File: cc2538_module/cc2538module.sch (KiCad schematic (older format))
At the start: 49 parts, among them CON1 USB-MICRO-B, J2 XBEE, P1 CONN_2, SW1 JS102011SCQN, U1 TPS769XX, U2 TPS6217X, U3 CC2538, X1 32MHZ, X2 32.768KHz, j9 JTAG

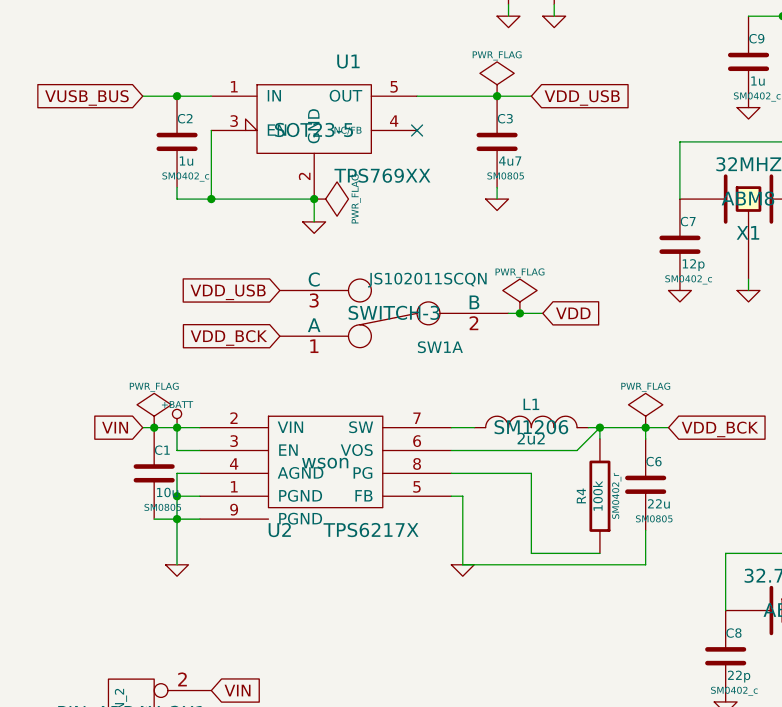
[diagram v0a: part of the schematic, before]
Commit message: Update component tolerances
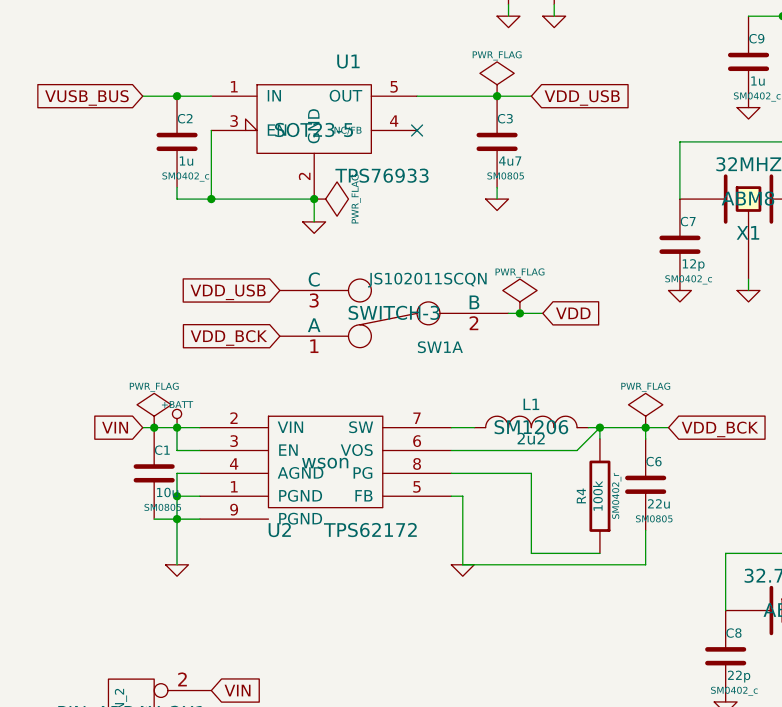
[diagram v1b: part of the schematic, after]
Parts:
- C10, C11, C12, C13, C14, C15, C16, C17, C18, C19, C20, C21, C22, C7, C8, C9: Voltage (none) -> 3.3
- C4, C5: Voltage (none) -> 5
- D1: Color (none) -> red; Voltage (none) -> ~1.6
- D2, D3: Color (none) -> green; Voltage (none) -> 2
- D4: Color (none) -> Green; Voltage (none) -> 2
- U1: value TPS769XX -> TPS76933; Voltage (none) -> 3.3
- U2: value TPS6217X -> TPS62172; Voltage (none) -> 3.3
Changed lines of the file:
@@
 LIBS:contrib
 LIBS:valves
+LIBS:cc2538
+LIBS:cc2538module-cache
+LIBS:jtagx7
+LIBS:tps6217x
 LIBS:w_connectors
-LIBS:cc2538
-LIBS:tps6217x
 LIBS:xbee
-LIBS:jtagx7
-LIBS:cc2538module-cache
 EELAYER 27 0
 EELAYER END
@@
 Sheet 1 1
 Title ""
-Date "30 jul 2014"
+Date "1 aug 2014"
 Rev ""
 Comp ""
@@
 F 2 "SM0402_c" H 2838 1600 30  0000 C CNN
 F 3 "~" H 2800 1750 60  0000 C CNN
+F 4 "5" H 2800 1750 60  0001 C CNN "Voltage"
 	1    2800 1750
 	1    0    0    -1
@@
 F 2 "SM0402_c" H 2638 1600 30  0000 C CNN
 F 3 "~" H 2600 1750 60  0000 C CNN
+F 4 "5" H 2600 1750 60  0001 C CNN "Voltage"
 	1    2600 1750
 	1    0    0    -1
@@
 F 2 "SM0402_c" H 3388 2850 30  0000 C CNN
 F 3 "~" H 3350 3000 60  0000 C CNN
+F 4 "3.3" H 3350 3000 60  0001 C CNN "Voltage"
 	1    3350 3000
 	1    0    0    -1
@@
 F 2 "SM0402_c" H 3988 2850 30  0000 C CNN
 F 3 "~" H 3950 3000 60  0000 C CNN
+F 4 "3.3" H 3950 3000 60  0001 C CNN "Voltage"
 	1    3950 3000
 	1    0    0    -1
@@
 F 2 "SM0402_c" H 3588 4650 30  0000 C CNN
 F 3 "~" H 3550 4800 60  0000 C CNN
+F 4 "3.3" H 3550 4800 60  0001 C CNN "Voltage"
 	1    3550 4800
 	1    0    0    -1
@@
 F 2 "SM0402_c" H 4188 4650 30  0000 C CNN
 F 3 "~" H 4150 4800 60  0000 C CNN
+F 4 "3.3" H 4150 4800 60  0001 C CNN "Voltage"
 	1    4150 4800
 	1    0    0    -1
@@
 F 2 "SM0402_c" H 3938 1400 30  0000 C CNN
 F 3 "~" H 3900 1550 60  0000 C CNN
+F 4 "3.3" H 3900 1550 60  0001 C CNN "Voltage"
 	1    3900 1550
 	1    0    0    -1
@@
 F 2 "SM0402_c" H 3688 2050 30  0000 C CNN
 F 3 "~" H 3650 2200 60  0000 C CNN
+F 4 "3.3" H 3650 2200 60  0001 C CNN "Voltage"
 	1    3650 2200
 	1    0    0    -1
@@
 F 2 "SM0402_c" H 7788 1100 30  0000 C CNN
 F 3 "~" H 7750 1250 60  0000 C CNN
+F 4 "3.3" H 7750 1250 60  0001 C CNN "Voltage"
 	1    7750 1250
 	1    0    0    -1
@@
 P 1750 2500
 F 0 "U1" H 1900 2800 60  0000 C CNN
-F 1 "TPS769XX" H 2050 2300 60  0000 C CNN
+F 1 "TPS76933" H 2050 2300 60  0000 C CNN
 F 2 "SOT23-5" H 1750 2500 60  0000 C CNN
 F 3 "~" H 1750 2500 60  0000 C CNN
+F 4 "3.3" H 1750 2500 60  0001 C CNN "Voltage"
 	1    1750 2500
 	1    0    0    -1
@@
 P 1800 3950
 F 0 "U2" H 1600 3650 60  0000 C CNN
-F 1 "TPS6217X" H 2000 3650 60  0000 C CNN
+F 1 "TPS62172" H 2000 3650 60  0000 C CNN
 F 2 "wson" H 1800 3950 60  0000 C CNN
 F 3 "~" H 1800 3950 60  0000 C CNN
+F 4 "3.3" H 1800 3950 60  0001 C CNN "Voltage"
 	1    1800 3950
 	1    0    0    -1
@@
 F 2 "LED-0603" H 1650 6500 60  0000 C CNN
 F 3 "~" H 1650 6500 60  0000 C CNN
+F 4 "~1.6" H 1650 6500 60  0001 C CNN "Voltage"
+F 5 "red" H 1650 6500 60  0001 C CNN "Color"
 	1    1650 6500
 	0    1    1    0
@@
 F 2 "LED-0603" H 1950 6500 60  0000 C CNN
 F 3 "~" H 1950 6500 60  0000 C CNN
+F 4 "2" H 1950 6500 60  0001 C CNN "Voltage"
+F 5 "green" H 1950 6500 60  0001 C CNN "Color"
 	1    1950 6500
 	0    1    1    0
@@
 F 2 "LED-0603" H 2250 6500 60  0000 C CNN
 F 3 "~" H 2250 6500 60  0000 C CNN
+F 4 "2" H 2250 6500 60  0001 C CNN "Voltage"
+F 5 "green" H 2250 6500 60  0001 C CNN "Color"
 	1    2250 6500
 	0    1    1    0
@@
 F 2 "LED-0603" H 2550 6500 60  0000 C CNN
 F 3 "~" H 2550 6500 60  0000 C CNN
+F 4 "2" H 2550 6500 60  0001 C CNN "Voltage"
+F 5 "Green" H 2550 6500 60  0001 C CNN "Color"
 	1    2550 6500
 	0    1    1    0
@@
 F 2 "SM0402_c" H 4038 5950 30  0000 C CNN
 F 3 "~" H 4000 6100 60  0000 C CNN
+F 4 "3.3" H 4000 6100 60  0001 C CNN "Voltage"
 	1    4000 6100
 	1    0    0    -1
@@
 F 2 "SM0402_c" H 4238 5950 30  0000 C CNN
 F 3 "~" H 4200 6100 60  0000 C CNN
+F 4 "3.3" H 4200 6100 60  0001 C CNN "Voltage"
 	1    4200 6100
 	1    0    0    -1
@@
 F 2 "SM0402_c" H 4438 5950 30  0000 C CNN
 F 3 "~" H 4400 6100 60  0000 C CNN
+F 4 "3.3" H 4400 6100 60  0001 C CNN "Voltage"
 	1    4400 6100
 	1    0    0    -1
@@
 F 2 "SM0402_c" H 4638 5950 30  0000 C CNN
 F 3 "~" H 4600 6100 60  0000 C CNN
+F 4 "3.3" H 4600 6100 60  0001 C CNN "Voltage"
 	1    4600 6100
 	1    0    0    -1
@@
 F 2 "SM0402_c" H 4838 5950 30  0000 C CNN
 F 3 "~" H 4800 6100 60  0000 C CNN
+F 4 "3.3" H 4800 6100 60  0001 C CNN "Voltage"
 	1    4800 6100
 	1    0    0    -1
@@
 F 2 "SM0402_c" H 5038 5950 30  0000 C CNN
 F 3 "~" H 5000 6100 60  0000 C CNN
+F 4 "3.3" H 5000 6100 60  0001 C CNN "Voltage"
 	1    5000 6100
 	1    0    0    -1
@@
 F 2 "SM0402_c" H 5238 5950 30  0000 C CNN
 F 3 "~" H 5200 6100 60  0000 C CNN
+F 4 "3.3" H 5200 6100 60  0001 C CNN "Voltage"
 	1    5200 6100
 	1    0    0    -1
@@
 F 2 "SM0402_c" H 5488 5950 30  0000 C CNN
 F 3 "~" H 5450 6100 60  0000 C CNN
+F 4 "3.3" H 5450 6100 60  0001 C CNN "Voltage"
 	1    5450 6100
 	1    0    0    -1
@@
 F 2 "SM0402_c" H 5738 5950 30  0000 C CNN
 F 3 "~" H 5700 6100 60  0000 C CNN
+F 4 "3.3" H 5700 6100 60  0001 C CNN "Voltage"
 	1    5700 6100
 	1    0    0    -1
